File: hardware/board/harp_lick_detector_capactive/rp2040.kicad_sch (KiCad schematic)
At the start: 28 parts

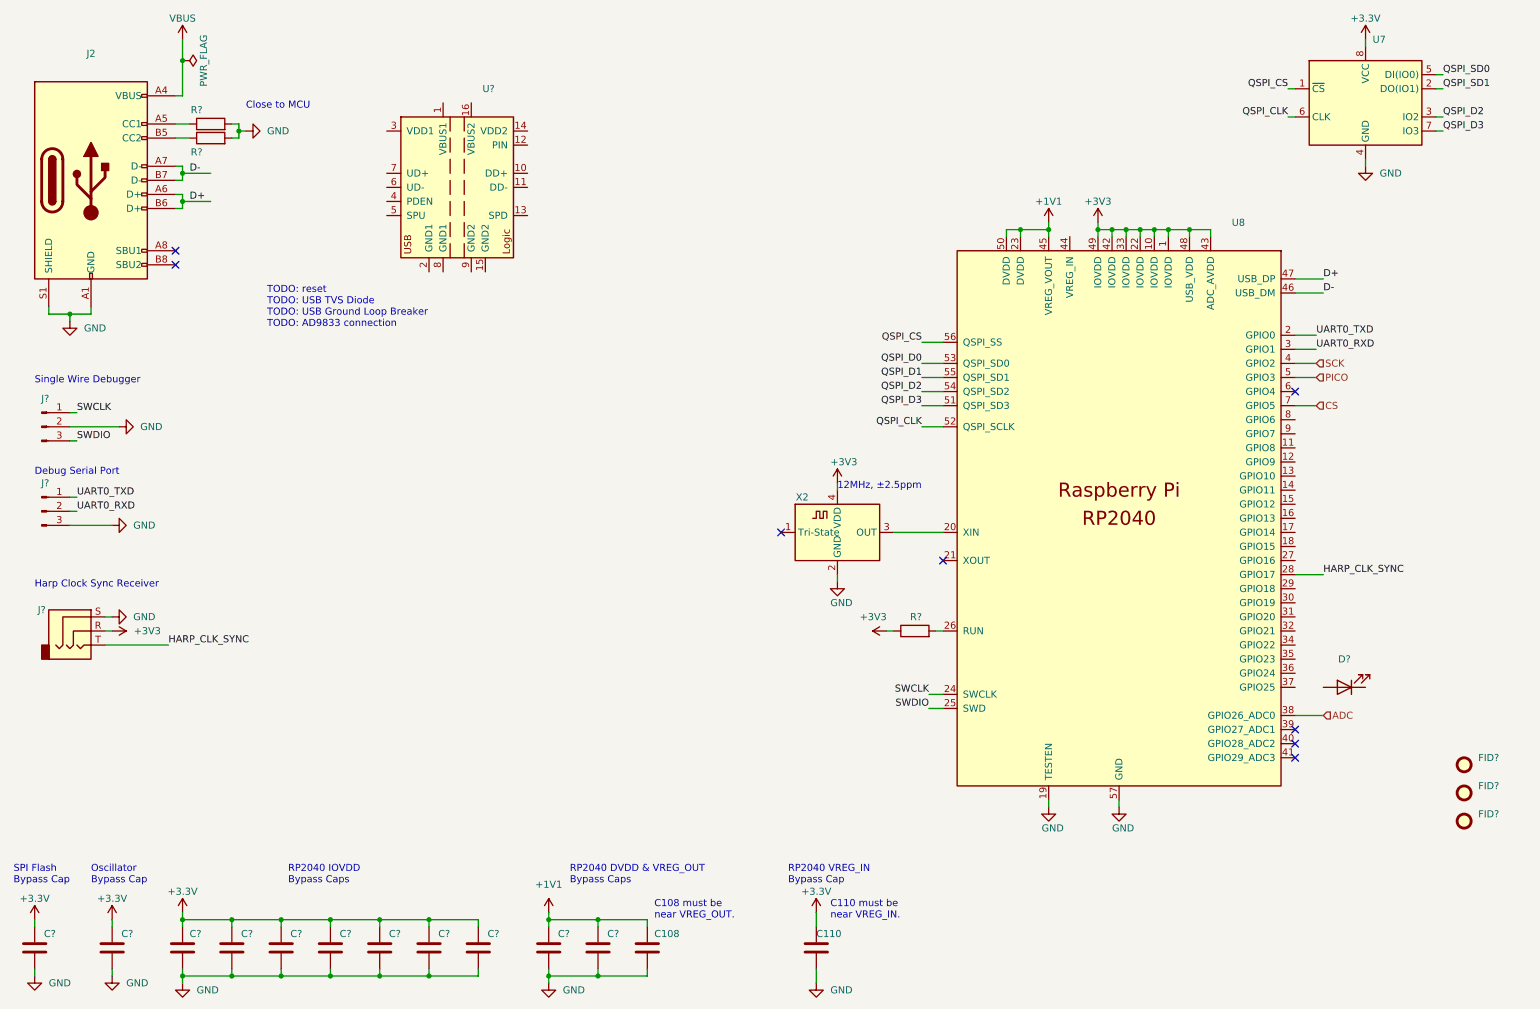
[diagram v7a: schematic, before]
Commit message: add usb isolator
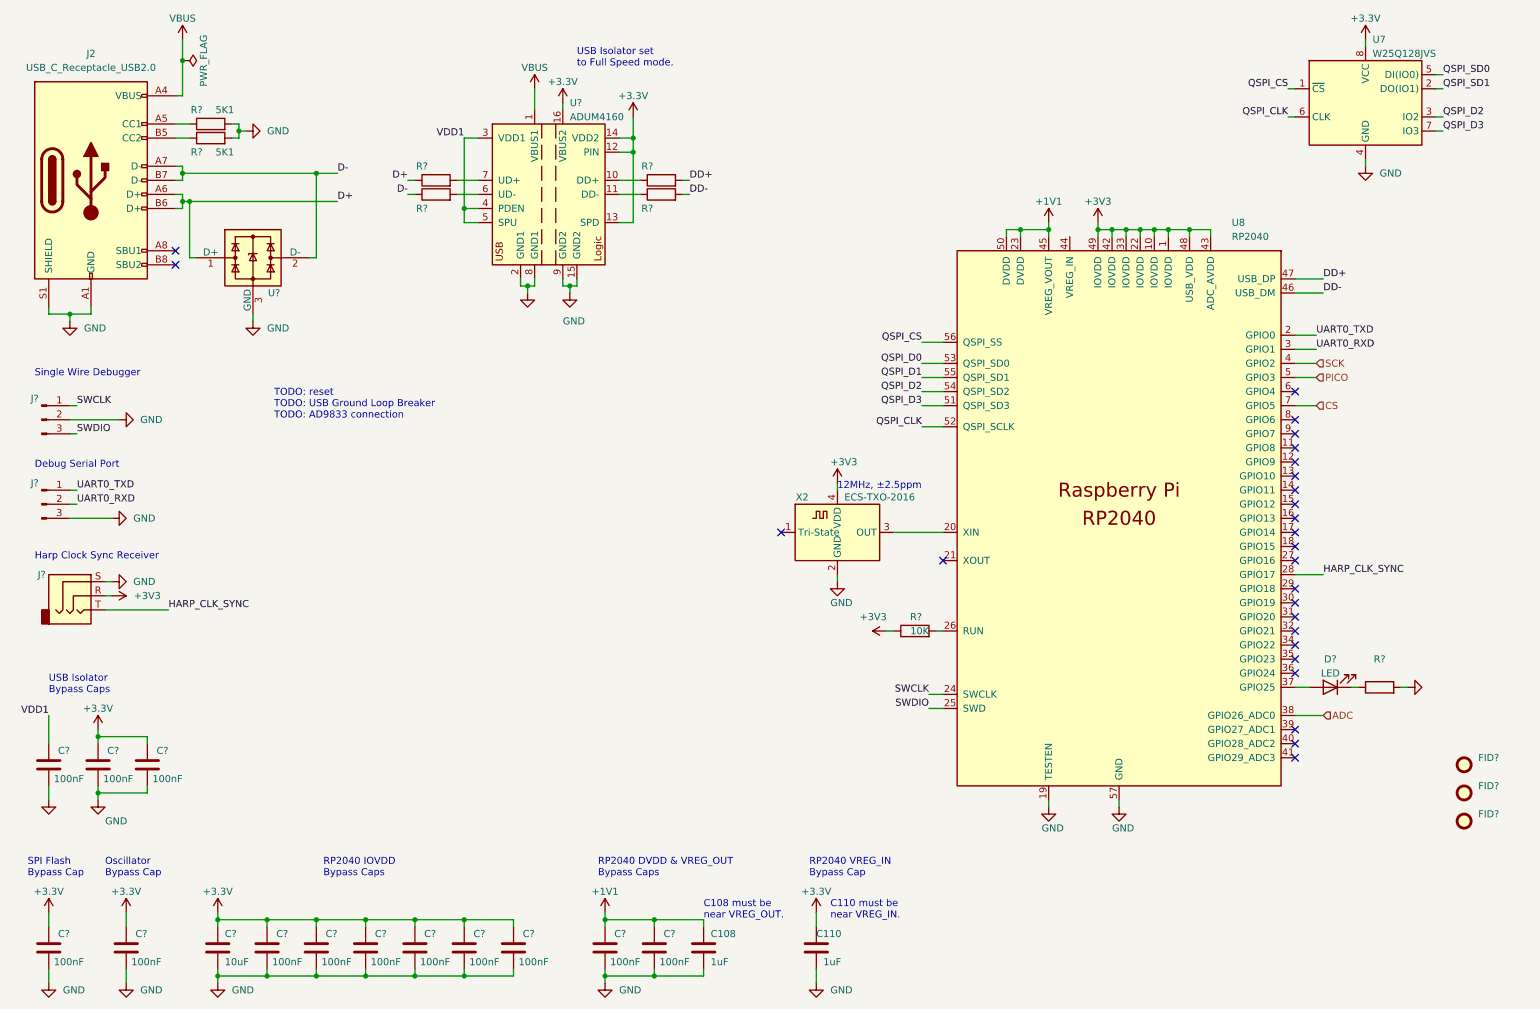
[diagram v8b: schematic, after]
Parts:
- added C? (x3): 100nF, Capacitor_SMD:C_0603_1608Metric_Pad1.08x0.95mm_HandSolder, symbol Device:C
- added R? (x5): (no value), symbol Device:R
- added U?: (no value), symbol Power_Protection:TPD2EUSB30
- C108, C110: value (none) -> 1uF; footprint (none) -> Capacitor_SMD:C_0603_1608Metric_Pad1.08x0.95mm_HandSolder
- C? (x10): value (none) -> 100nF; footprint (none) -> Capacitor_SMD:C_0603_1608Metric_Pad1.08x0.95mm_HandSolder
- C?: value (none) -> 10uF; footprint (none) -> Capacitor_SMD:C_0805_2012Metric
- D?: value (none) -> LED
- FID? (x2): value (none) -> ~; footprint (none) -> Fiducial:Fiducial_0.5mm_Mask1mm
- FID?: value (none) -> Fiducial; footprint (none) -> Fiducial:Fiducial_0.5mm_Mask1mm
- J2: value (none) -> USB_C_Receptacle_USB2.0; footprint (none) -> Connector_USB:USB_C_Receptacle_Amphenol_12401610E4-2A_CircularHoles
- J?: value (none) -> AudioJack3
- J?: value (none) -> Conn_01x03_Male
- J?: value (none) -> ~
- R? (x2): value (none) -> 5K1; footprint (none) -> Resistor_SMD:R_0603_1608Metric_Pad0.98x0.95mm_HandSolder
- R?: value (none) -> 10K; footprint (none) -> Resistor_SMD:R_0402_1005Metric_Pad0.72x0.64mm_HandSolder
- U7: value (none) -> W25Q128JVS; footprint (none) -> Package_SO:SOIC-8_5.23x5.23mm_P1.27mm
- U8: value (none) -> RP2040; footprint (none) -> RP2040_minimal:RP2040-QFN-56
- U?: value (none) -> ADUM4160; footprint (none) -> Package_SO:SOIC-16W_7.5x10.3mm_P1.27mm
- X2: value (none) -> ECS-TXO-2016; footprint (none) -> Crystal:Crystal_SMD_2016-4Pin_2.0x1.6mm
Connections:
- net +3V3: now also U?.12 (PIN), U?.13 (SPD), U?.14 (VDD2), U?.16 (VBUS2), C?.2, C?.2
- net D+: now also R?.1, U?.1 (D+); no longer U8.47 (USB_DP)
- net D-: now also R?.1, U?.2 (D-); no longer U8.46 (USB_DM)
- net GND: now also U?.15 (GND2), U?.9 (GND2), C?.1, C?.1, R?.2, U?.3 (GND)
- net VBUS: now also U?.1 (VBUS1)
- net at U8.37 (GPIO25): now also D?.2 (A)
- net at U?.10 (DD+): now also R?.1
- net at U?.11 (DD-): now also R?.1
- net GND1: now reaches U?.2 (GND1)
- net GND1: now also U?.8 (GND1), C?.1
- net VDD1: now reaches U?.3 (VDD1)
- net VDD1: now also U?.4 (PDEN), U?.5 (SPU), C?.2
- net at U?.6 (UD-): now also R?.2
- net at U?.7 (UD+): now also R?.2
- net at D?.1 (K): now also R?.1
- new net DD+: R?.2, U8.47 (USB_DP)
- new net DD-: R?.2, U8.46 (USB_DM)
- no-connect marks 8 -> 26
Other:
- note added: "TODO: reset TODO: USB Ground Loop Breaker TODO: AD9833 connection"
- note added: "USB Isolator Bypass Caps"
- note added: "USB Isolator set to Full Speed mode."
- note removed: "Close to MCU"
- note removed: "TODO: reset TODO: USB TVS Diode TODO: USB Ground Loop Breaker TODO: AD9833 connection"
- moved on the sheet: C108, C?, D?, J?, U?
